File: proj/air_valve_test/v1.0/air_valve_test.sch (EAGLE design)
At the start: 4 parts, among them U1 BEAGLEBONE_OUTLINE

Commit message: exploring air valves + fans for edu brain
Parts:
- removed FAN3: OD4020-24HSS, openag-fans:OD4020-24HSS
- removed U1: BEAGLEBONE_OUTLINE, openag-microcontrollers:BEAGLEBONE_OUTLINE
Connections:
- removed net FAN2+: FAN3.+
- removed net FAN2-: FAN3.-
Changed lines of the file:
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@@
 <setting verticaltext="up"/>
 </settings>
-<grid distance="0.1" unitdist="inch" unit="inch" style="lines" multiple="1" display="no" altdistance="0.01" altunitdist="inch" altunit="inch"/>
+<grid distance="1.5" unitdist="inch" unit="inch" style="lines" multiple="1" display="yes" altdistance="0.1" altunitdist="inch" altunit="inch"/>
 <layers>
 <layer number="1" name="Top" color="4" fill="1" visible="no" active="no"/>
@@
 <attribute name="URL" value="https://github.com/OpenAgInitiative/openag_eagle/proj/edu_brain"/>
 </part>
-<part name="U1" library="openag-microcontrollers" deviceset="BEAGLEBONE_OUTLINE" device=""/>
 <part name="FAN1" library="openag-fans" deviceset="OD4020-24HSS" device="" value="OD4020-24HSS"/>
-<part name="FAN3" library="openag-fans" deviceset="OD4020-24HSS" device="" value="OD4020-24HSS"/>
 </parts>
 <sheets>
@@
 <wire x1="228.6" y1="114.3" x2="228.6" y2="76.2" width="0.254" layer="97" style="longdash"/>
 <wire x1="228.6" y1="76.2" x2="152.4" y2="76.2" width="0.254" layer="97" style="longdash"/>
-<text x="157.48" y="148.59" size="1.778" layer="97">Fan w/Surface Mount L-Brackets, 24V, 1.7W, 9.0CFM, 32dB</text>
-<wire x1="152.4" y1="114.3" x2="152.4" y2="152.4" width="0.254" layer="97" style="longdash"/>
-<wire x1="152.4" y1="152.4" x2="228.6" y2="152.4" width="0.254" layer="97" style="longdash"/>
-<wire x1="228.6" y1="152.4" x2="228.6" y2="114.3" width="0.254" layer="97" style="longdash"/>
 <wire x1="228.6" y1="114.3" x2="152.4" y2="114.3" width="0.254" layer="97" style="longdash"/>
 </plain>
 <instances>
 <instance part="FRAME1" gate="G$1" x="152.4" y="0"/>
-<instance part="U1" gate="G$1" x="342.9" y="76.2"/>
 <instance part="FAN1" gate="G$1" x="190.5" y="93.98"/>
-<instance part="FAN3" gate="G$1" x="190.5" y="132.08"/>
 </instances>
 <busses>
@@
 </segment>
 </net>
-<net name="FAN2+" class="0">
-<segment>
-<pinref part="FAN3" gate="G$1" pin="+"/>
-<wire x1="175.26" y1="132.08" x2="172.72" y2="132.08" width="0.1524" layer="91"/>
-<label x="172.72" y="132.08" size="1.778" layer="95" rot="R180" xref="yes"/>
-</segment>
-</net>
-<net name="FAN2-" class="0">
-<segment>
-<pinref part="FAN3" gate="G$1" pin="-"/>
-<wire x1="205.74" y1="132.08" x2="208.28" y2="132.08" width="0.1524" layer="91"/>
-<label x="208.28" y="132.08" size="1.778" layer="95" xref="yes"/>
-</segment>
-</net>

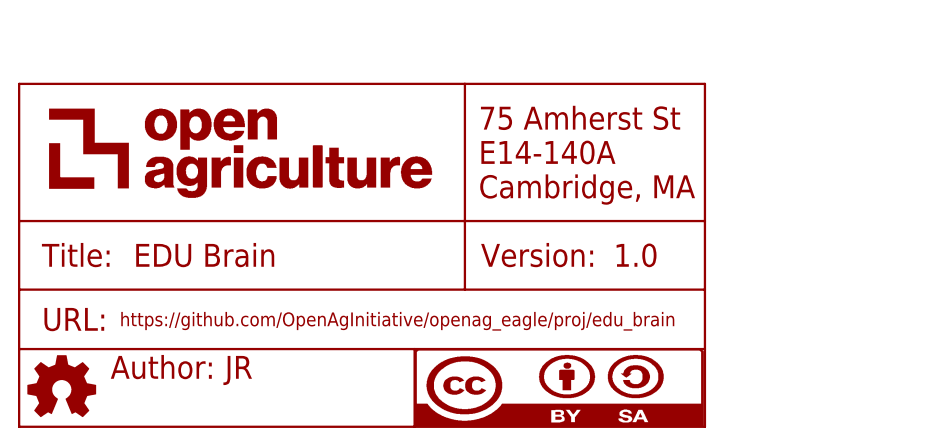
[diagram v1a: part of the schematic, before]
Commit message: finalized air valve test pcb
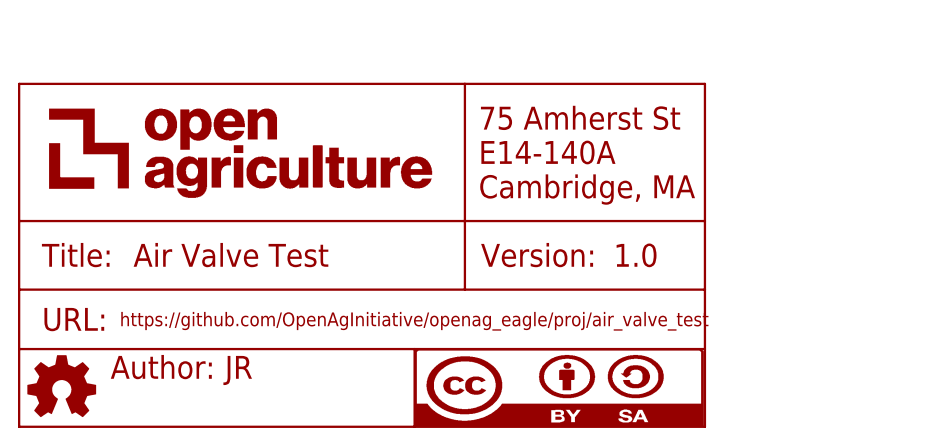
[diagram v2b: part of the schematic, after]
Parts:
- FRAME1: DESCRIPTION Top Brain for PFC-EDU -> Fan + valve test for pfc edu brain; TITLE EDU Brain -> Air Valve Test; URL https://github.com/OpenAgInitiative/openag_eagle/proj/edu_b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 -> https://github.com/OpenAgInitiative/openag_eagle/proj/air_v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
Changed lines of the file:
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@@
 <setting verticaltext="up"/>
 </settings>
-<grid distance="1.5" unitdist="inch" unit="inch" style="lines" multiple="1" display="yes" altdistance="0.1" altunitdist="inch" altunit="inch"/>
+<grid distance="0.1" unitdist="inch" unit="inch" style="lines" multiple="1" display="no" altdistance="0.01" altunitdist="inch" altunit="inch"/>
 <layers>
 <layer number="1" name="Top" color="4" fill="1" visible="no" active="no"/>
@@
 <part name="FRAME1" library="openag-frames" deviceset="DOCFIELD" device="">
 <attribute name="AUTHOR" value="JR"/>
-<attribute name="DESCRIPTION" value="Top Brain for PFC-EDU"/>
-<attribute name="TITLE" value="EDU Brain"/>
-<attribute name="URL" value="https://github.com/OpenAgInitiative/openag_eagle/proj/edu_brain"/>
+<attribute name="DESCRIPTION" value="Fan + valve test for pfc edu brain"/>
+<attribute name="TITLE" value="Air Valve Test"/>
+<attribute name="URL" value="https://github.com/OpenAgInitiative/openag_eagle/proj/air_valve_test"/>
 </part>
 <part name="FAN1" library="openag-fans" deviceset="OD4020-24HSS" device="" value="OD4020-24HSS"/>
